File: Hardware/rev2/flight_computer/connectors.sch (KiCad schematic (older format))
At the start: 15 parts, among them J10 Conn_02x01, J4 JST_8_RA, J5 JST_GH_6_RA, J6 JST_GH_4_RA, J7 JST_GH_5_RA, J8 Conn_02x03, J9 Conn_02x03, U4 Dual_XOR_GATE, U5 Dual_XOR_GATE

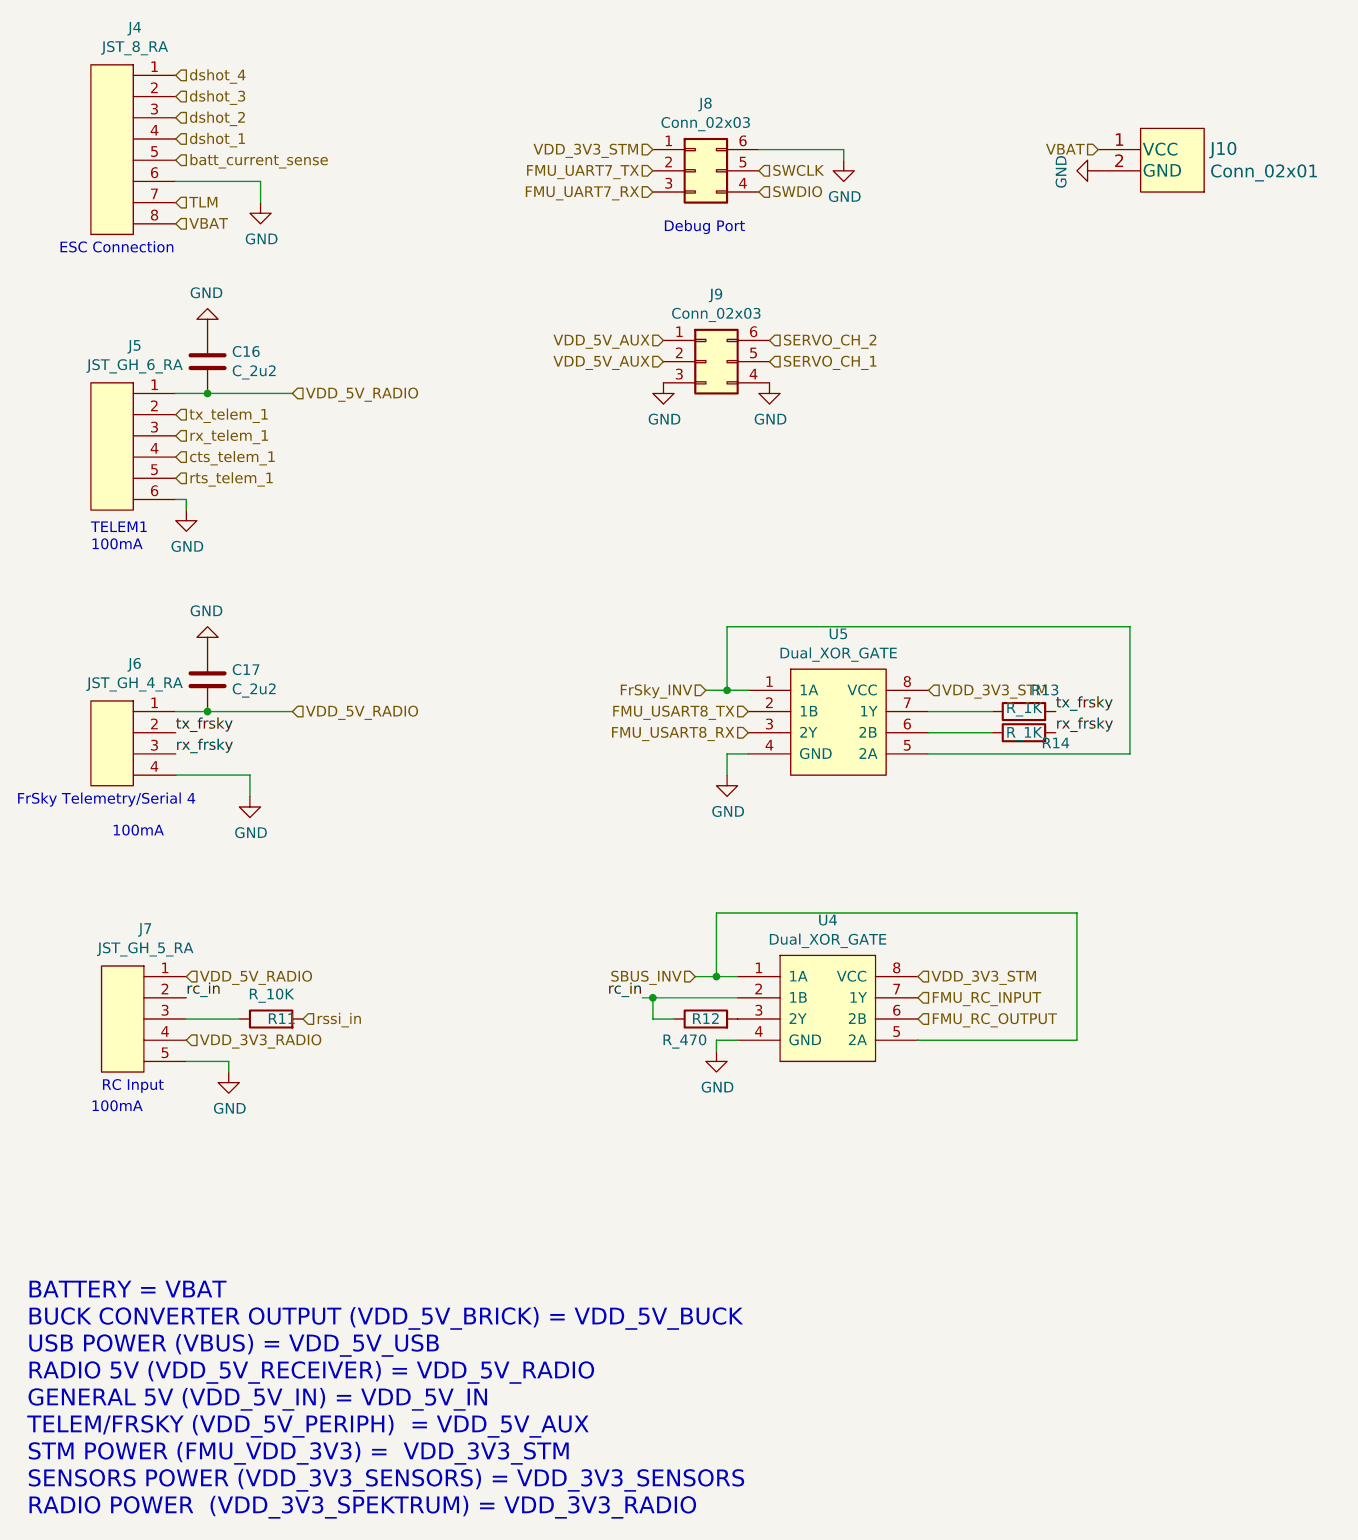
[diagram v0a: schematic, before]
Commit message: Removes frysky + spektrum connectors
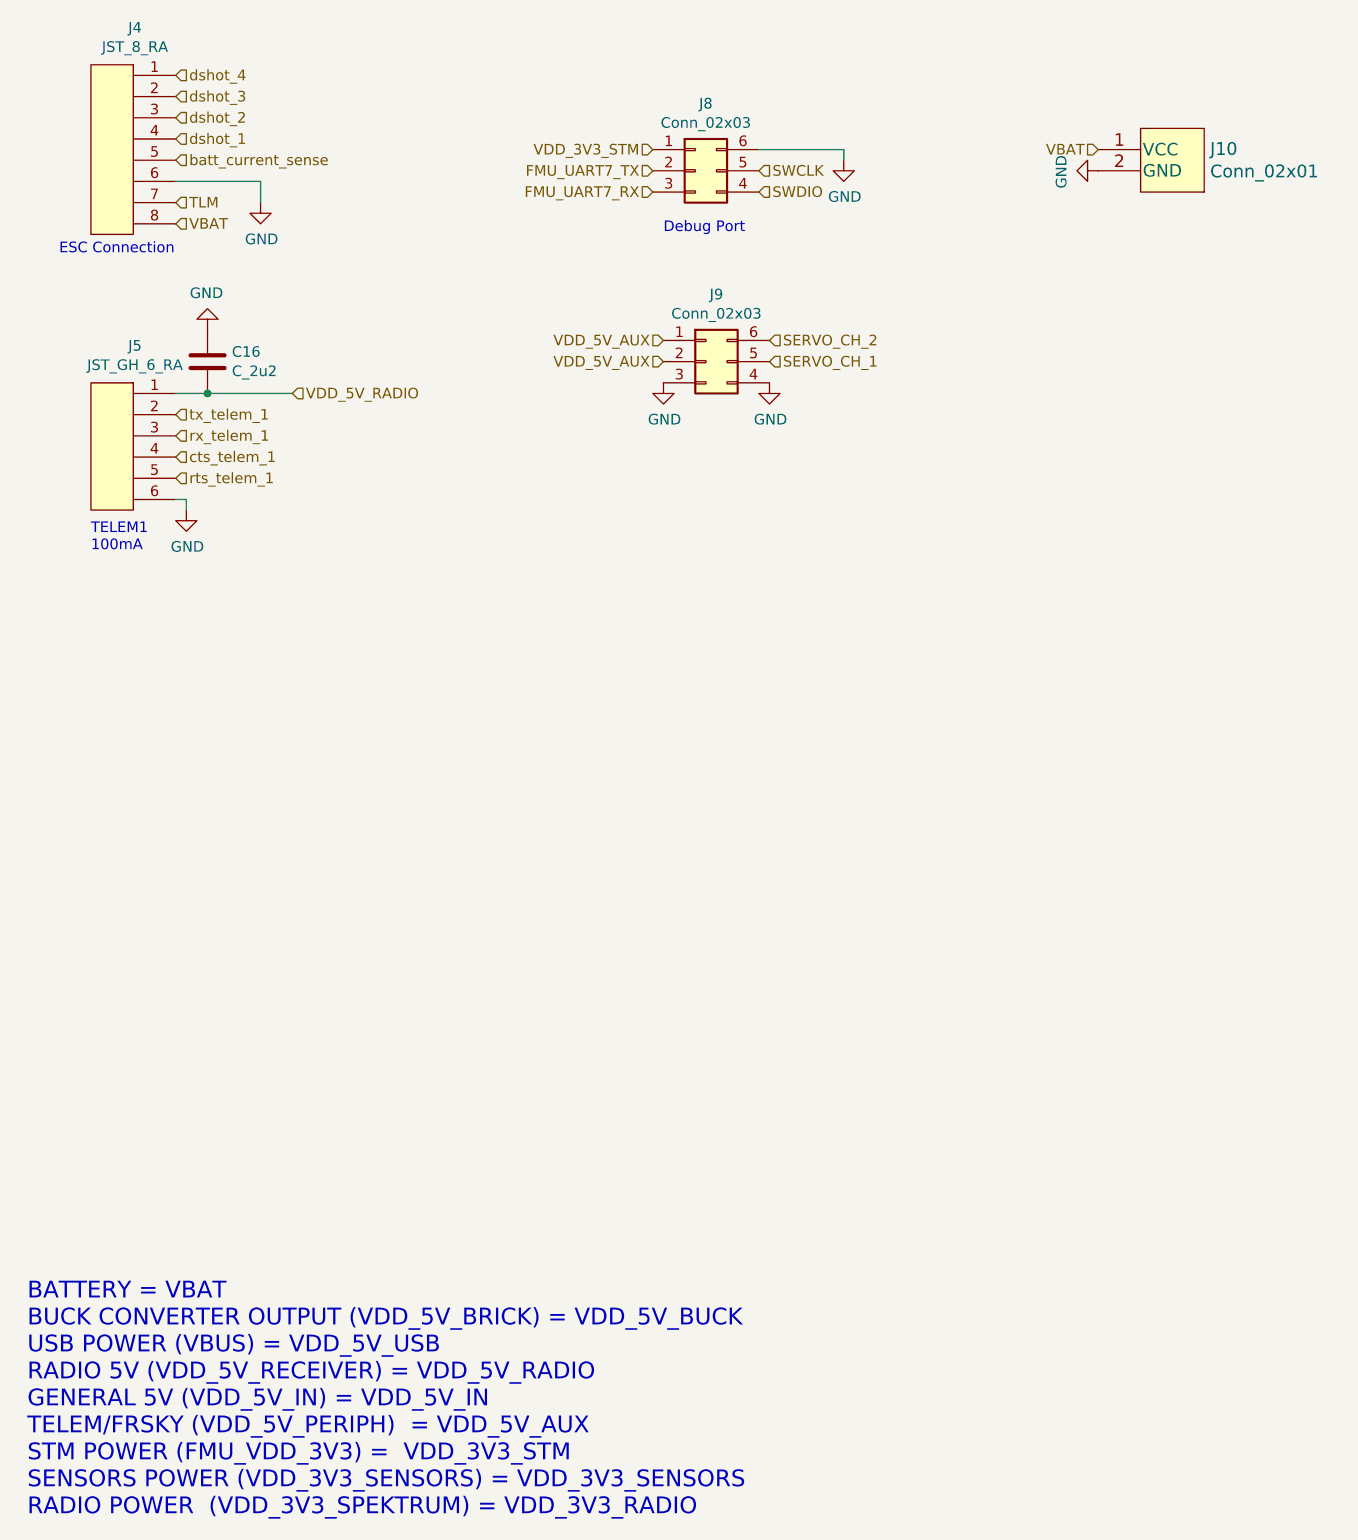
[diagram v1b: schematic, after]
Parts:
- removed C17: C_2u2, Capacitors_SMD:C_0805, symbol openDrone_parts:C_2u2
- removed J6: JST_GH_4_RA, drone_footprints:JST_SM04B-GHS-TB(LF)(SN)-, symbol openDrone_parts:JST_GH_4_RA
- removed J7: JST_GH_5_RA, drone_footprints:SM05B-GHS-TBLFSN, symbol openDrone_parts:JST_GH_5_RA
- removed R11: R_10K, Resistors_SMD:R_0805, symbol openDrone_parts:R_10K
- removed R12: R_470, Resistors_SMD:R_0805, symbol openDrone_parts:R_470
- removed R13, R14: R_1K, Resistors_SMD:R_0805, symbol openDrone_parts:R_1K
- removed U4, U5: Dual_XOR_GATE, Housings_SSOP:TSSOP-8_3x3mm_Pitch0.65mm, symbol openDrone_parts:Dual_XOR_GATE
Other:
- note removed: "100mA"
- note removed: "FrSky Telemetry/Serial 4\n"
- note removed: "RC Input"

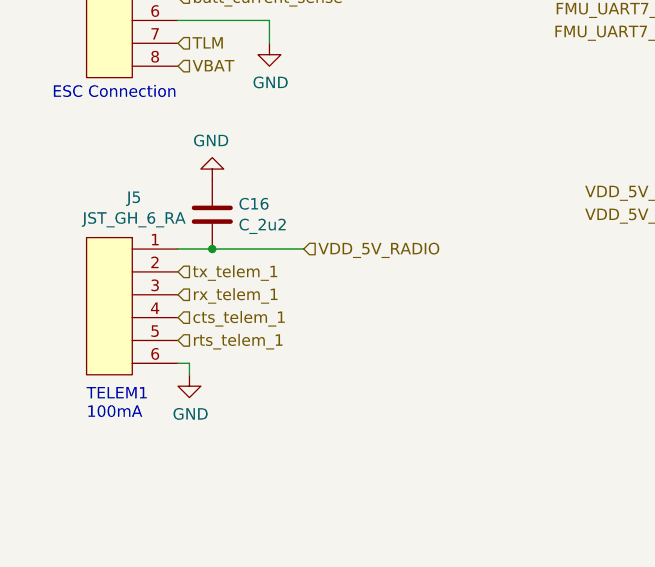
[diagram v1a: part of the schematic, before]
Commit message: Fixes telemetry uart and dshot
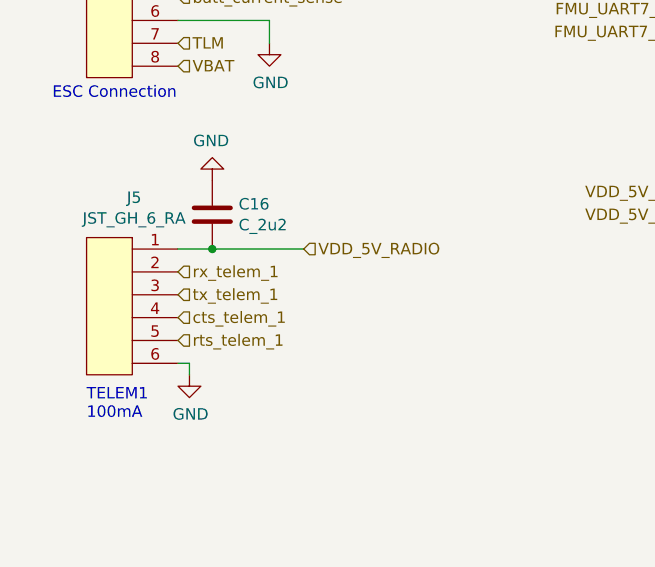
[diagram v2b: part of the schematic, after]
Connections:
- net rx_telem_1: now also J5.2; no longer J5.3
- net tx_telem_1: now also J5.3; no longer J5.2
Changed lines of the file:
@@
 Text Notes 1000 3050 0    50   ~ 0
 TELEM1\n100mA
+Text HLabel 1400 2500 2    50   Input ~ 0
+tx_telem_1
 Text HLabel 1400 2400 2    50   Input ~ 0
-tx_telem_1
-Text HLabel 1400 2500 2    50   Input ~ 0
 rx_telem_1
 Text HLabel 1400 2600 2    50   Input ~ 0
